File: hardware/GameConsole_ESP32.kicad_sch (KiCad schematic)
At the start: 17 parts, among them J1 Conn_01x20_Socket, J2 Conn_01x20_Socket, J3 Conn_01x05, SW1 RedBtn, SW2 GreenBtn, SW3 YellowBtn, SW4 BlueBtn, U1 I2C OLED

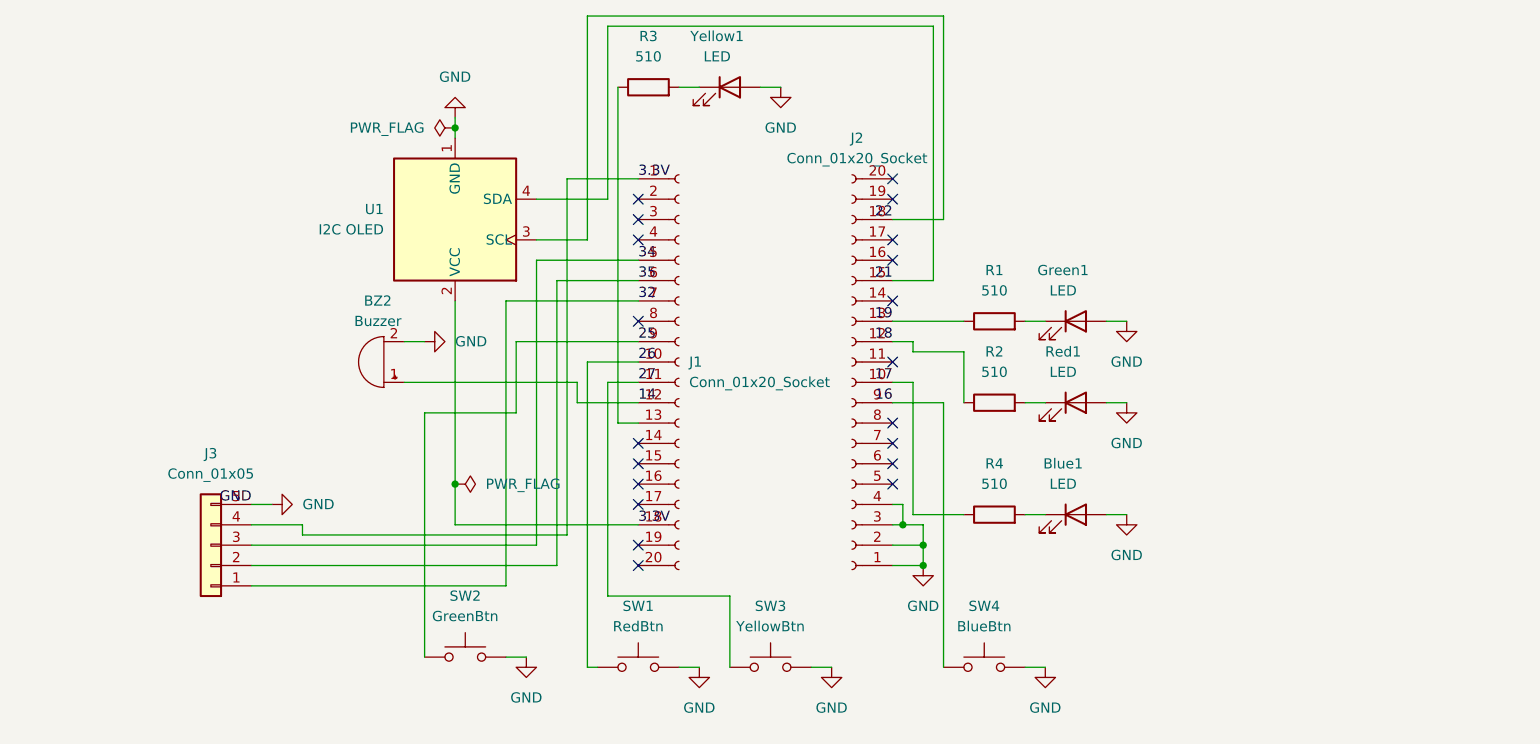
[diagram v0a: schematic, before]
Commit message: Cleaned up schematic and updated PCB design
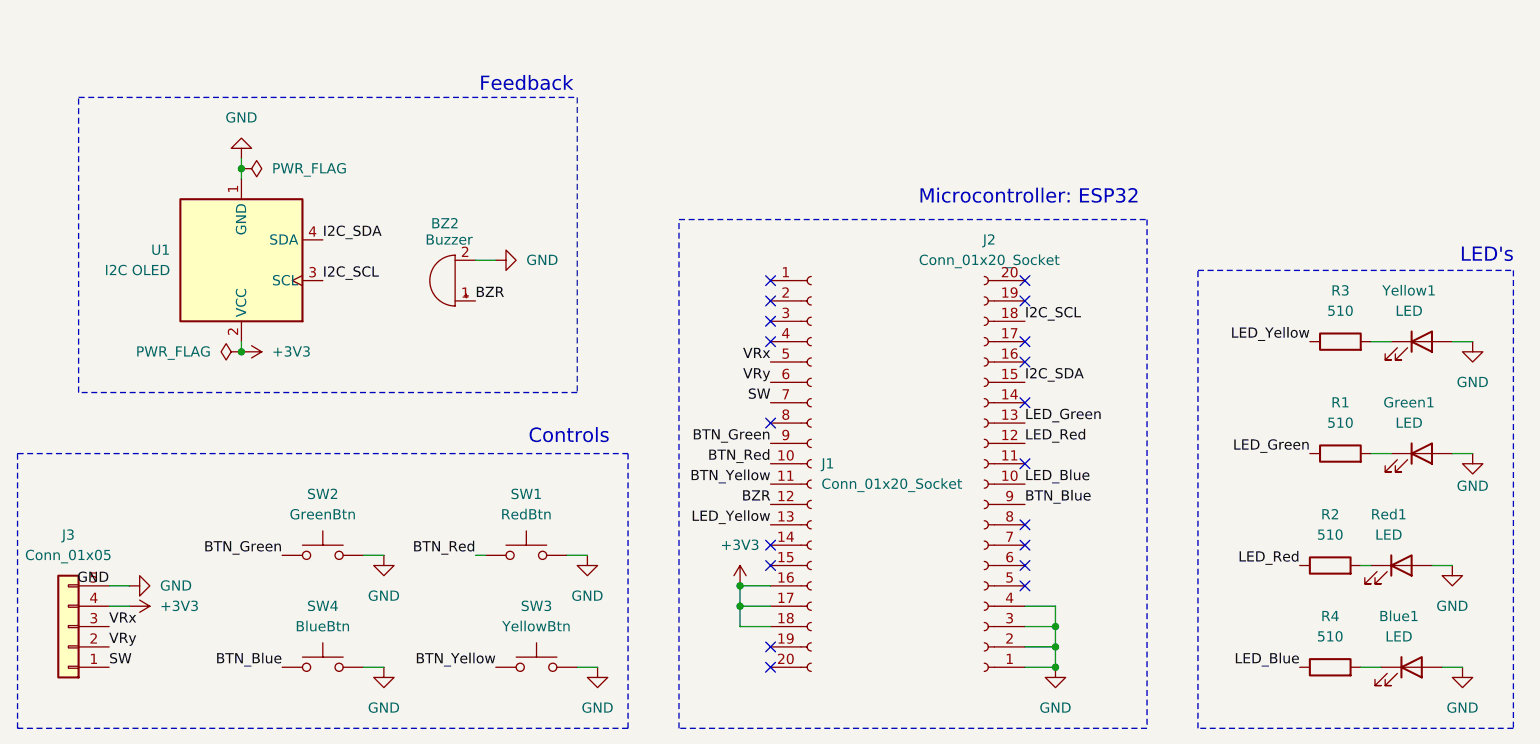
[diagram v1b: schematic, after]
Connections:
- net LED_Yellow: now reaches J1.13 (Pin_13), R3.1
- net +3V3: now reaches J1.16 (Pin_16)
- net +3V3: now also J1.17 (Pin_17), J1.18 (Pin_18), J3.4 (Pin_4), U1.2 (VCC)
- net 14 renamed BZR
- net 16 renamed BTN_Blue
- net 17 renamed LED_Blue
- net 18 renamed LED_Red
- net 19 renamed LED_Green
- net 21 renamed I2C_SDA
- net 22 renamed I2C_SCL
- net 25 renamed BTN_Green
- net 26 renamed BTN_Red
- net 27 renamed BTN_Yellow
- removed net 3.3V: J1.1 (Pin_1), J1.18 (Pin_18), J3.4 (Pin_4), U1.2 (VCC)
- net 32 renamed SW
- net 34 renamed VRx
- net 35 renamed VRy
- no-connect marks 20 -> 19
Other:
- note added: "Controls"
- note added: "Feedback"
- note added: "LED's"
- note added: "Microcontroller: ESP32"
- title: (none) -> ESP32 Game Console
- moved on the sheet: BZ2, Blue1, Green1, J1, J2, J3, R1, R2, R3, R4, Red1, SW1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
